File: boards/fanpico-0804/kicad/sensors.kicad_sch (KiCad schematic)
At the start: 8 parts, among them J16 Sensor1, J17 Sensor2

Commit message: New PCB revision v1.3
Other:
- title: FanPico-0804 v1.2 -> FanPico-0804 v1.3
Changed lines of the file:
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@@
   (paper "A4")
   (title_block
-    (title "FanPico-0804 v1.2")
-    (date "2022-03-11")
+    (title "FanPico-0804 v1.3")
+    (date "2022-04-10")
     (company "Timo Kokkonen <tjko@iki.fi>")
     (comment 3 "Fanpico firmware reference PCB.")

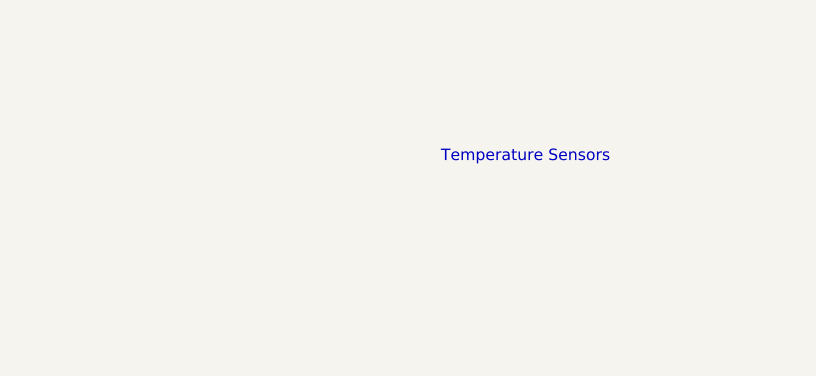
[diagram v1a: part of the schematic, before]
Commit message: Cleanup schematic (no actual changes that affect PCB).
- Add labels to sub-pages so printed schematic is more readable.
- Rename FANx_PWM_READ to MBFANx_PWM_READ
- Rename FANx_TACHO_GEN to MBFANx_TACHO_GEN
- Use standard (KiCAD) footprints for the ICs (U1-U3)
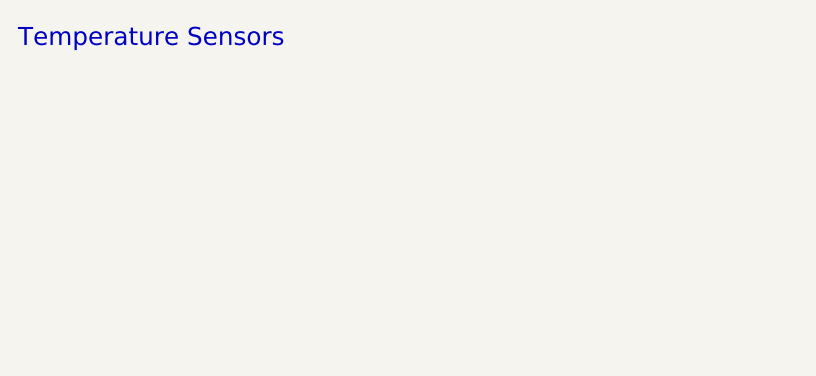
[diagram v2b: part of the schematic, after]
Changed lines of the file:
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@@
   (title_block
     (title "FanPico-0804 v1.3")
-    (date "2022-04-10")
+    (date "2022-08-18")
     (company "Timo Kokkonen <tjko@iki.fi>")
     (comment 3 "Fanpico firmware reference PCB.")
@@
     (stroke (width 0) (type default) (color 0 0 0 0))
   )
-  (text "Temperature Sensors" (at 66.04 30.48 0)
-    (effects (font (size 1.27 1.27)) (justify left bottom))
+  (text "Temperature Sensors" (at 19.05 17.78 0)
+    (effects (font (size 2 2)) (justify left bottom))
   )
   (global_label "AGND" (shape input) (at 135.89 121.92 0) (fields_autoplaced)
